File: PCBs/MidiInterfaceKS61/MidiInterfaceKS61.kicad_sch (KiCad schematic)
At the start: 82 parts, among them CN13 Conn_01x13_Male, CN14 Conn_01x12_Male, J3 Conn_01x20_Female, J4 Conn_01x20_Female, J5 Conn_01x01_Male

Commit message: V1.1 PCB updates after initial testing 1. Share data out line between LCD, 7 Segment and button scan to yield spare io lines for    control of WS8212 LEDs for music stand lamp 2. Replace level shifting FET on Button Driver PCBs by resistor 3. Generate combined ks61,button driver & button mount prototype PCB for economic testing with JLC PCB
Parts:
- added J6: LAMP, Connector_PinHeader_2.54mm:PinHeader_2x03_P2.54mm_Vertical, symbol Connector_Generic:Conn_02x03_Odd_Even
- added POT1: Conn_01x02_Male, Connector_PinHeader_2.54mm:PinHeader_1x02_P2.54mm_Vertical, symbol Connector:Conn_01x02_Male
- RD32: value 4k7 -> 3K3
- RU14, RU15, RU32: value 4k7* -> 4k7
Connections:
- net 3V3: now also POT1.2 (Pin_2)
- net 5V: now also J6.5 (Pin_5), J6.6 (Pin_6)
- net PA13: now also J6.4 (Pin_4); no longer SEG7.3 (Pin_3)
- net PA14: now also J6.3 (Pin_3); no longer SEG7.4 (Pin_4)
- net PB10: now also SEG7.4 (Pin_4); no longer Buttons1.3 (Pin_3)
- net PB7: now also Buttons1.3 (Pin_3), SEG7.3 (Pin_3)
- net GND renamed 0V
- net 0V: now also J6.1 (Pin_1), J6.2 (Pin_2), POT1.1 (Pin_1)
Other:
- note added: "Notes: 1. For M-Audio Keystation61 Mk3 fit CN13/CN14 (2mm pitch). For pedalboard fit Pedal and Expression connectors as required. 2. J3 Pin20 is 0V on STM32F103 Blue Pill and 5V on STM32F401/411 Black pill. Set solder bridge STM32 if required. 3. Fit pullup/pulldown only if reqd. If 3.3V pullups are needed, fit voltage divider pulldown/pullup resistors in appropriate ratio. e.g. 3k3 pull down 1k7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"
- note added: "V1.0 Initial release V1.1 Adopt common data line PB7/SDL for LCD, Buttons, 7Seg to yield 2 i/o lines Add Lamp connector to control WS2812 LED strip on Music stand Add Potentiometer 0v,3V3 connector to power ADC pot inputs"
- note removed: "Notes: 1. For M-Audio Keystation61 Mk3 fit CN13/CN14 (2mm pitch). For pedalboard fit Pedal and Expression connectors as required. 2. J3 Pin20 is 0V on STM32F103 Blue Pill and 5V on STM32F401/411 Black pill. Set solder bridge STM32 if required. 3. Where mixed pullups to 3.3V and 5V are needed, fit voltage divider pulldown/pullup resistors in appropriate ratio. e.g. 3k3 pull down 1k7 pull up"
- moved on the sheet: J5, ToDebugx2

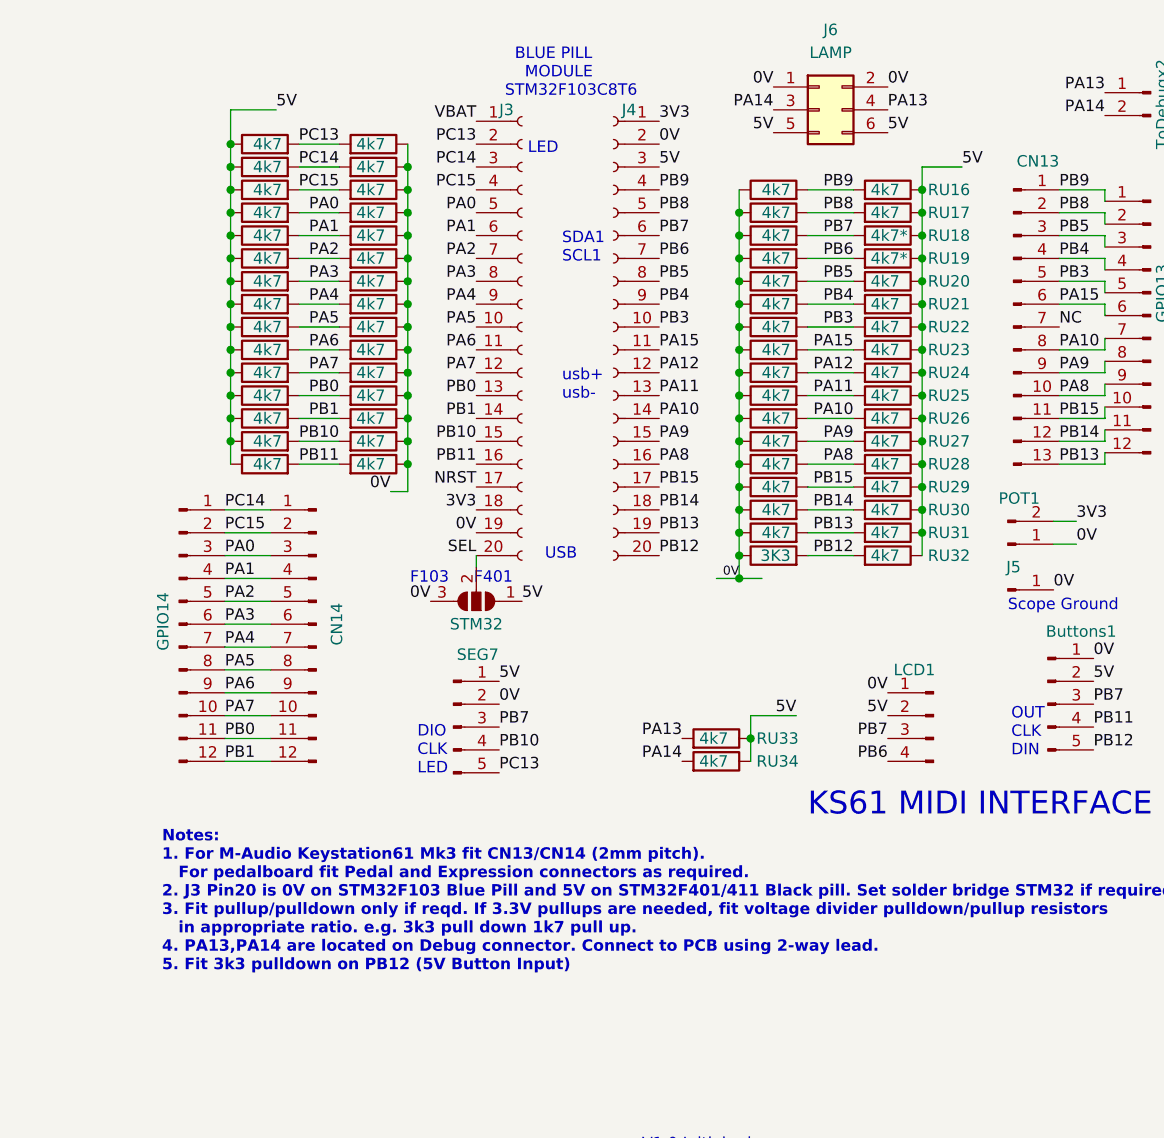
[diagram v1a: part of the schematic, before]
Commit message: Updates during initial console construction
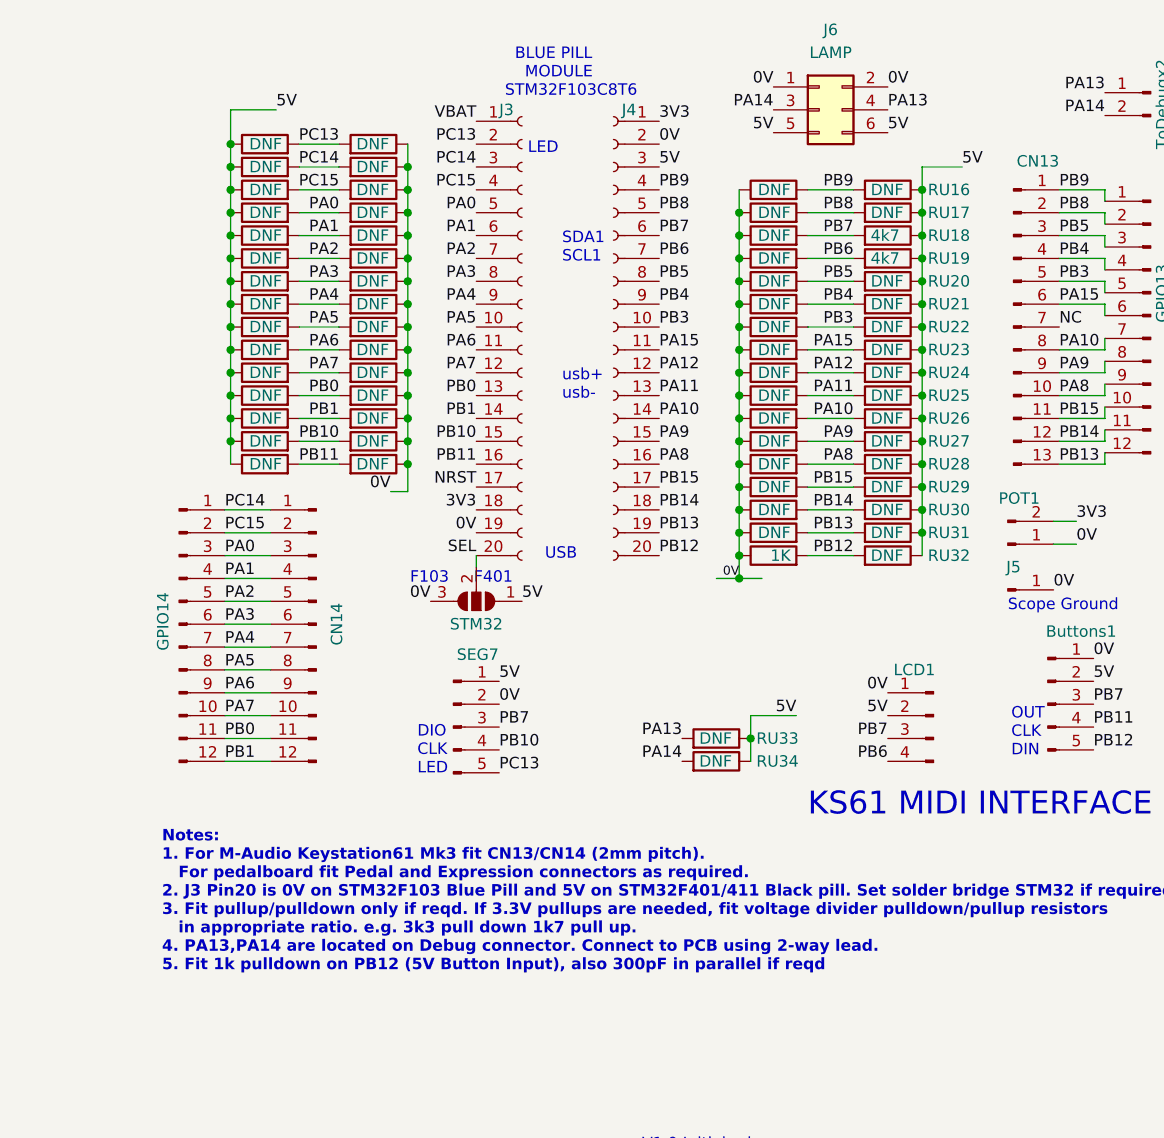
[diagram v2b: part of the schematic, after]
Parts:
- RD1, RD10, RD11, RD12, RD13, RD14, RD15, RD16, RD17, RD18, RD19, RD2, RD20, RD21, RD22, RD23, RD24, RD25, RD26, RD27, RD28, RD29, RD3, RD30, RD31, RD4, RD5, RD6, RD7, RD8, RD9, RU1, RU10, RU11, RU12, RU13, RU14, RU15, RU16, RU17, RU2, RU20, RU21, RU22, RU23, RU24, RU25, RU26, RU27, RU28, RU29, RU3, RU30, RU31, RU32, RU33, RU34, RU4, RU5, RU6, RU7, RU8, RU9: value 4k7 -> DNF
- RD32: value 3K3 -> 1K
- RU18, RU19: value 4k7* -> 4k7
